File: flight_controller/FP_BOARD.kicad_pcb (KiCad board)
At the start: 2 copper layers, 100 x 100 mm, 252 parts, among them CN1 A1251WV-S-6P, CN2 A1251WV-S-4P, CN3 A1251WV-S-3P, J1 HX PZ2.54-3X4P ZZ, J10 A2012WV-S-9P, J11 A1257WV-S-6P-LCP, J12 A1257WV-S-6P-LCP, J13 A1257WV-S-6P-LCP, J14 HR911105A_C12074, J15 A1257WV-S-6P-LCP, J16 HCZZ0494-2, J17 TYPE-C16PIN2MD(073) (USB TYPE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, J2 B3B-ZR-SM4-TF(LF)(SN), J3 HX PZ2.54-3X4P ZZ, J4 HX PZ2.54-3X4P ZZ, J5 SM04B-SRSS-TB(LF)(SN), J6 A1257WV-S-6P-LCP, J7 HCZZ0494-4, J8 HCZZ0494-4, J9 A1257WV-S-6P-LCP, Q1 AO3400A, SW1 6.0*6.0*6.0, SW2 6.0*6.0*6.0, U1 HB-PH9-12727PB2GOB, U10 24LC64-I/SN, U11 FM25V02A-GTR, U12 MPU6500, U13 MS561101BA03-50, U14 LAN8742AI-CZ, U15 SN74LVC1G07DBVR_C19829659, U2 STM32H743IIT6, U3 HB-PH9-12727PB2GOB, U4 STM32F103C8T6, U5 SN74LVC2G240DCTR, U7 TJA1051T/3/1J, U8 TJA1051T/3/1J, U9 W25Q512JVFIQ, X1 XKXEL89CLI-SUAYLC-32.768K, X2 XL2EL89CLI-111YLC-16M, X3 X322524MLB4SI_C5210646, X4 XL2EL89CMI-111YLC-25M

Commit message: Placment in progress
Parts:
- moved R41 769.3 mm to (97.8, 42.6), turned to 180 degrees
- moved J2 741.5 mm to (97.5, 36.7), turned to 180 degrees
- moved R32 693.1 mm to (158.0, 48.6), turned to 180 degrees
- moved J1 687.2 mm to (149.2, 49.1), turned to 90 degrees
- moved R28 621.2 mm to (234.7, 31.9)
- moved R27 619.9 mm to (234.8, 35.1)
- moved R30 615.1 mm to (239.3, 35.6)
- moved U5 613.5 mm to (238.2, 26.4)
- moved R29 608.6 mm to (239.3, 32.1)
- moved C37 604.0 mm to (260.8, 24.7)
- moved J4 604.0 mm to (239.0, 45.2)
- moved R26 604.0 mm to (235.1, 57.6)
- moved R34 604.0 mm to (260.4, 52.3)
- moved R36 604.0 mm to (268.9, 29.8)
- moved R40 604.0 mm to (264.3, 52.3)
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
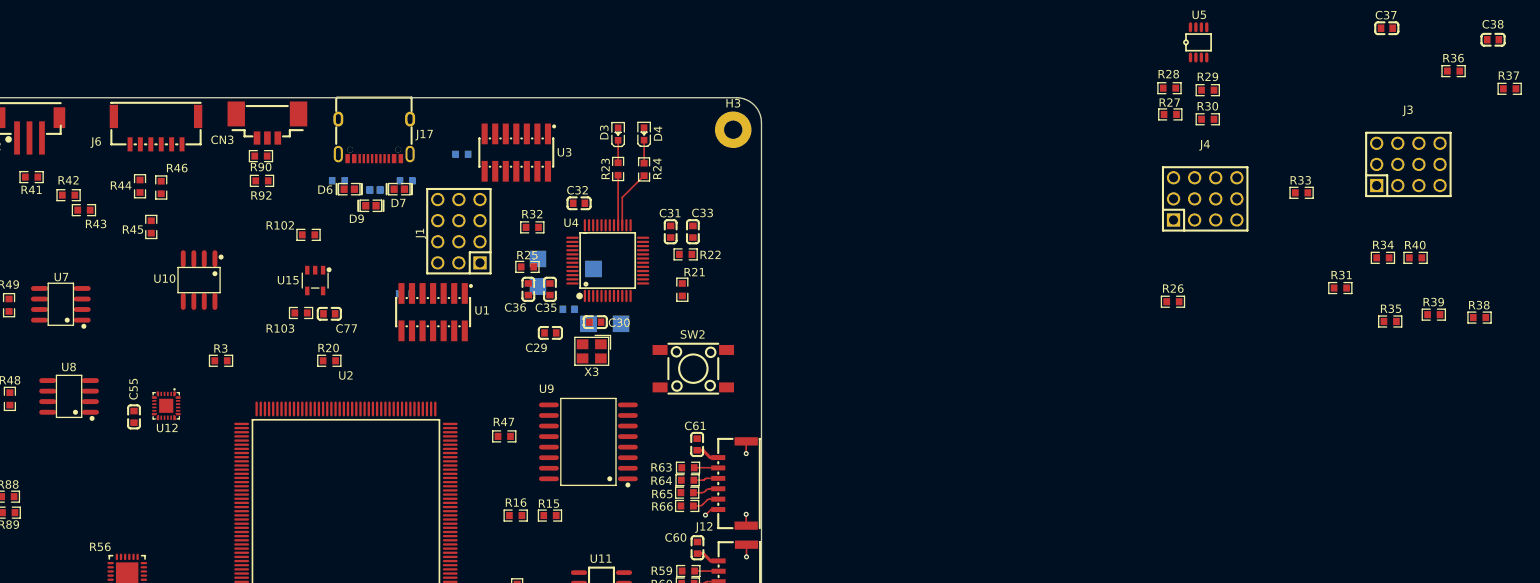
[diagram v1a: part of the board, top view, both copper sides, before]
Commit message: Almost done with placement , fixed some 3d models , fixed r56 to u56
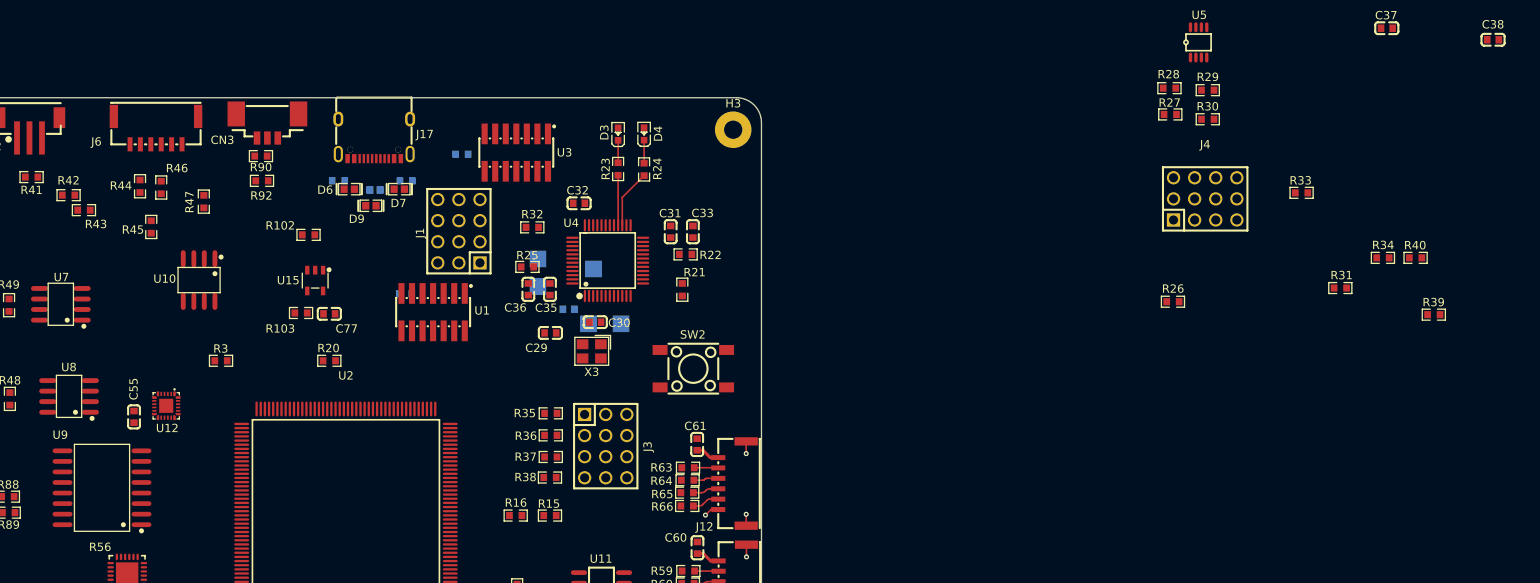
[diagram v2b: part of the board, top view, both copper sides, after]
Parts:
- moved R37 123.6 mm to (160.2, 76.3)
- moved R36 117.1 mm to (160.2, 73.7)
- moved R38 113.5 mm to (160.2, 78.8)
- moved J3 102.4 mm to (166.9, 75.0), turned to -90 degrees
- moved R35 101.6 mm to (160.2, 71.0)
- moved U9 58.8 mm to (106.2, 80.0)
- moved R47 45.9 mm to (118.5, 45.5), turned to 90 degrees

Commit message: Finished placement
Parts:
- removed R56: ICM-20689, easyeda2kicad:QFN-24_L4.0-W4.0-P0.50-TL-EP2.6
- added U56: ICM-20689, easyeda2kicad:QFN-24_L4.0-W4.0-P0.50-TL-EP2.6, F.Cu at (107.4, 91.1)
- C1, C2, R10, R15, R16, R17, R18, R92, R93, TP1, TP10, TP11, TP12, TP2, TP3, TP4, TP5, TP6, TP7, TP8, TP9, X1: moved to B.Cu
- moved C38 180.7 mm to (93.5, 40.7)
- moved TP11 159.1 mm to (151.7, 74.3), turned to 180 degrees
- moved TP8 153.8 mm to (151.4, 87.8), turned to 180 degrees
- moved R52 153.7 mm to (108.5, 117.5), turned to -90 degrees
- moved C54 151.8 mm to (113.0, 73.6), turned to 90 degrees
- moved R51 151.8 mm to (115.5, 77.5), turned to -90 degrees
- moved C17 151.0 mm to (125.6, 68.0)
- moved C50 149.6 mm to (120.5, 60.0), turned to 180 degrees
- moved TP4 149.0 mm to (144.7, 92.5), turned to 180 degrees
- moved TP9 148.9 mm to (151.6, 82.8), turned to 180 degrees
- moved R7 147.8 mm to (154.4, 67.0)
- moved TP10 147.5 mm to (144.1, 79.2), turned to 180 degrees
- moved TP6 147.4 mm to (151.4, 91.3), turned to 180 degrees
- moved TP12 147.2 mm to (149.8, 77.8), turned to 180 degrees
- moved R54 145.9 mm to (109.1, 103.0)
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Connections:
- Card1 pad 1: /SDMMC2_D2 -> /SENSORS/SDMMC2_D2
- Card1 pad 2: /SDMMC2_D3 -> /SENSORS/SDMMC2_D3
- Card1 pad 3: /SDMMC2_CMD -> /SENSORS/SDMMC2_CMD
- Card1 pad 5: /SDMMC2_CLK -> /SENSORS/SDMMC2_CLK
- Card1 pad 7: /SDMMC2_D0 -> /SENSORS/SDMMC2_D0
- Card1 pad 8: /SDMMC2_D1 -> /SENSORS/SDMMC2_D1
- Card1 pad 9: /SD_CARD_DETECT -> /SENSORS/SD_CARD_DETECT
- D8 pad 2: /USB_OTG_FS_DM -> /USB_OTG_FS_D-
- D9 pad 2: /USB_OTG_FS_DP -> /USB_OTG_FS_D+
- J17 pad 5: /USB_OTG_FS_DM -> /USB_OTG_FS_D-
- J17 pad 6: /USB_OTG_FS_DP -> /USB_OTG_FS_D+
- J17 pad 7: /USB_OTG_FS_DM -> /USB_OTG_FS_D-
- J17 pad 8: /USB_OTG_FS_DP -> /USB_OTG_FS_D+
- R50 pad 1: /SDMMC2_D2 -> /SENSORS/SDMMC2_D2
- R51 pad 1: /QUADSPI_BK1_NCS -> /SENSORS/QUADSPI_BK1_NCS
- R52 pad 1: /SDMMC2_D3 -> /SENSORS/SDMMC2_D3
- R53 pad 1: /SDMMC2_CMD -> /SENSORS/SDMMC2_CMD
- R54 pad 1: /SDMMC2_D0 -> /SENSORS/SDMMC2_D0
- R55 pad 1: /SDMMC2_D1 -> /SENSORS/SDMMC2_D1
- R57 pad 1: /I2C2_SDA -> /SENSORS/I2C2_SDA
- R58 pad 1: /I2C2_SCL -> /SENSORS/I2C2_SCL
- U10 pad 5: /I2C3_SDA -> /SENSORS/I2C3_SDA_EEPROM
- U10 pad 6: /I2C3_SCL -> /SENSORS/I2C3_SCL_EEPROM
- U11 pad 1: /SPI5_nCS1 -> /SENSORS/SPI5_nCS1
- U11 pad 2: /SPI5_MISO -> /SENSORS/SPI5_MISO
- U11 pad 5: /SPI5_MOSI -> /SENSORS/SPI5_MOSI
- U11 pad 6: /SPI5_SCK -> /SENSORS/SPI5_SCK
- U12 pad 12: /SPI2_DRDY2_INT2 -> /SENSORS/SPI2_DRDY2_INT2
- U12 pad 22: /SPI2_nCS1 -> /SENSORS/SPI2_nCS1
- U12 pad 23: /SPI2_SCK -> /SENSORS/SPI2_SCK
- U12 pad 24: /SPI2_MOSI -> /SENSORS/SPI2_MOSI
- U12 pad 9: /SPI2_MISO -> /SENSORS/SPI2_MISO
- U13 pad 7: /I2C2_SDA -> /SENSORS/I2C2_SDA
- U13 pad 8: /I2C2_SCL -> /SENSORS/I2C2_SCL
- U2 pad 122: /USB_OTG_FS_DM -> /STM32H7/USB_OTG_FS_D-
- U2 pad 123: /USB_OTG_FS_DP -> /STM32H7/USB_OTG_FS_D+
- U9 pad 1: /QUADSPI_BK1_IO3 -> /SENSORS/QUADSPI_BK1_IO3
- U9 pad 15: /QUADSPI_BK1_IO0 -> /SENSORS/QUADSPI_BK1_IO0
- U9 pad 16: /QUADSPI_CLK -> /SENSORS/QUADSPI_CLK
- U9 pad 7: /QUADSPI_BK1_NCS -> /SENSORS/QUADSPI_BK1_NCS
- U9 pad 8: /QUADSPI_BK1_IO1 -> /SENSORS/QUADSPI_BK1_IO1
- U9 pad 9: /QUADSPI_BK1_IO2 -> /SENSORS/QUADSPI_BK1_IO2
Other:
- copper layers 2 -> 6

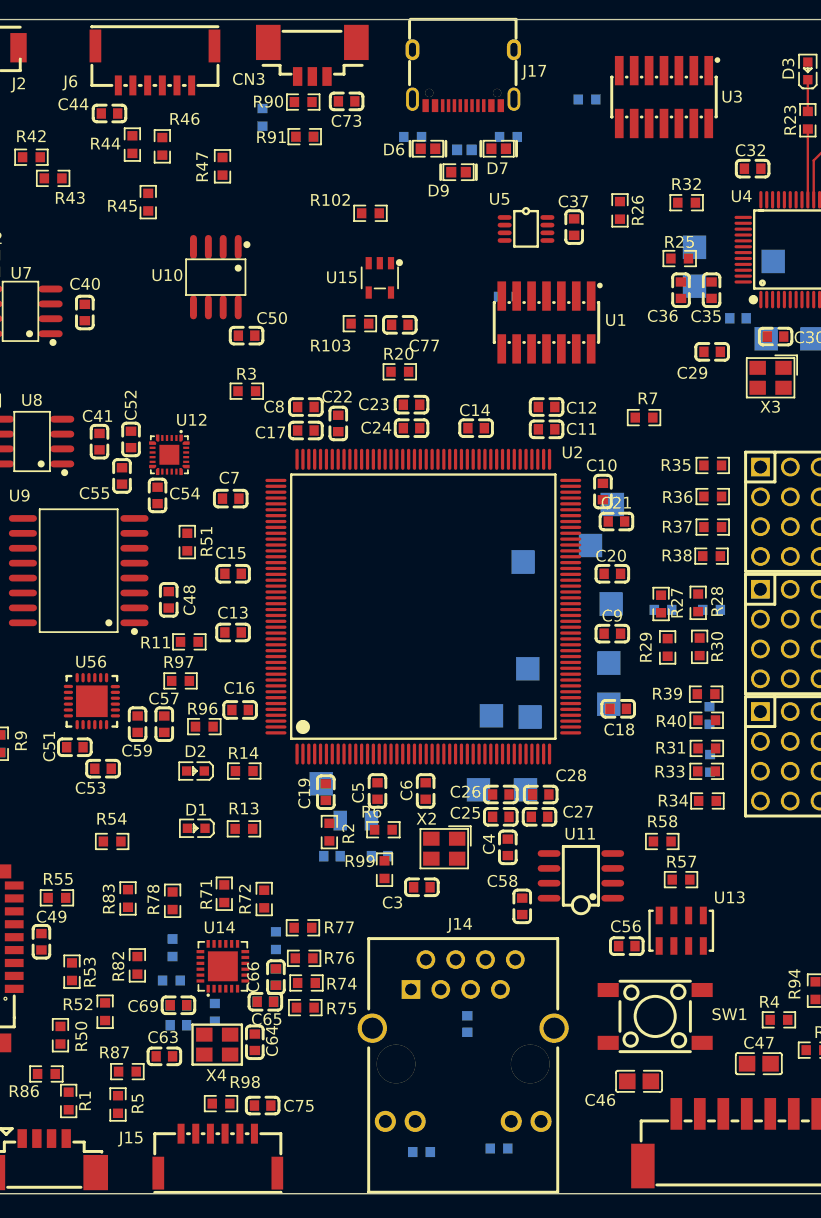
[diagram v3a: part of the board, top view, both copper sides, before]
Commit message: moved all to components to top
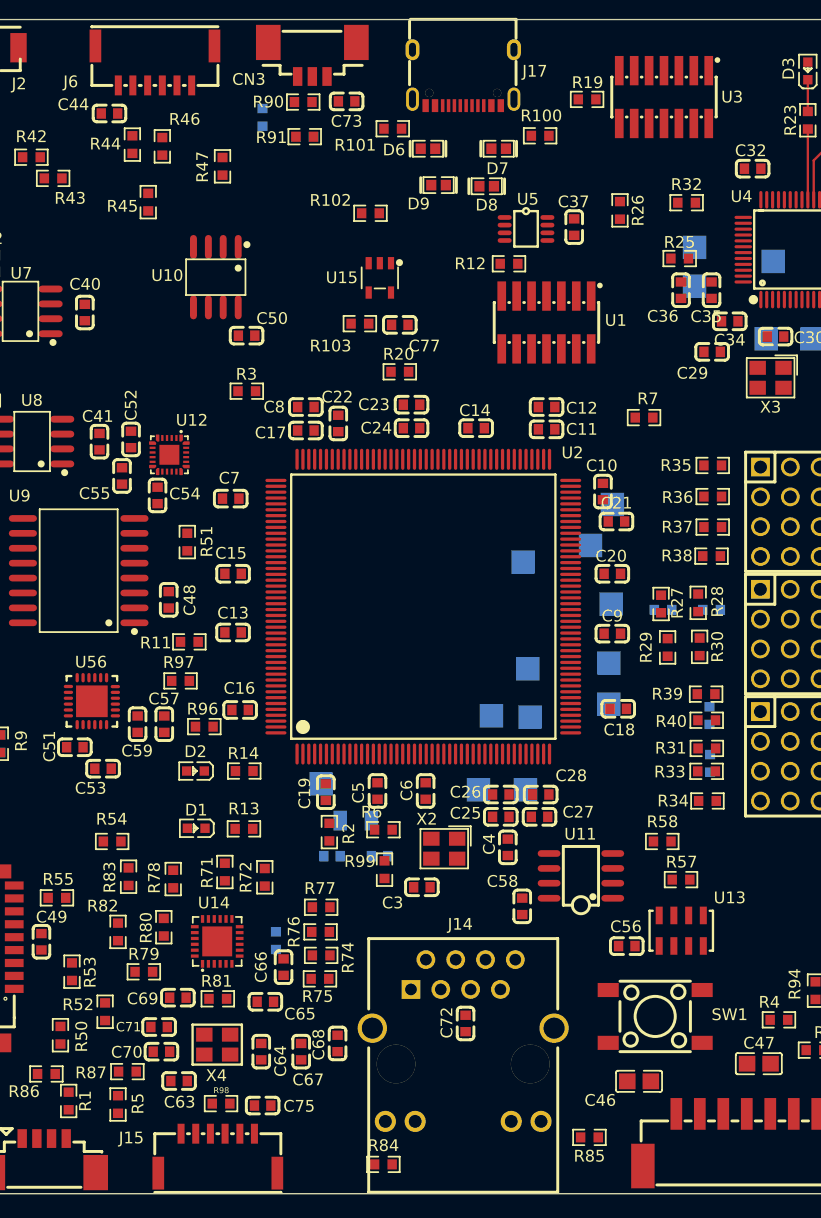
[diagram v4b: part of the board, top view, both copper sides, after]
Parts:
- C34, C67, C68, C70, C71, C72, D8, R100, R101, R12, R19, R79, R80, R81, R84, R85: moved to F.Cu
- moved R85 7.76 mm to (149.8, 128.2), turned to 180 degrees
- moved C68 7.71 mm to (128.3, 120.2)
- moved C67 5.23 mm to (125.2, 121.0), turned to 90 degrees
- moved C70 4.21 mm to (113.3, 121.0), turned to 180 degrees
- moved D8 3.64 mm to (141.0, 47.2), turned to 180 degrees
- moved R84 3.42 mm to (132.2, 130.6), turned to 0 degrees
- moved R82 3.29 mm to (109.6, 110.8)
- moved R12 2.80 mm to (142.9, 53.9), turned to 0 degrees
- moved R75 2.75 mm to (126.8, 114.8)
- moved R100 2.70 mm to (145.6, 43.0), turned to 0 degrees
- moved R74 2.66 mm to (126.9, 112.8)
- moved R76 2.65 mm to (126.8, 110.8)
- moved R79 2.47 mm to (111.8, 114.2), turned to 0 degrees
- moved C63 2.44 mm to (114.8, 123.5)
- moved R77 2.34 mm to (126.9, 108.7)
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
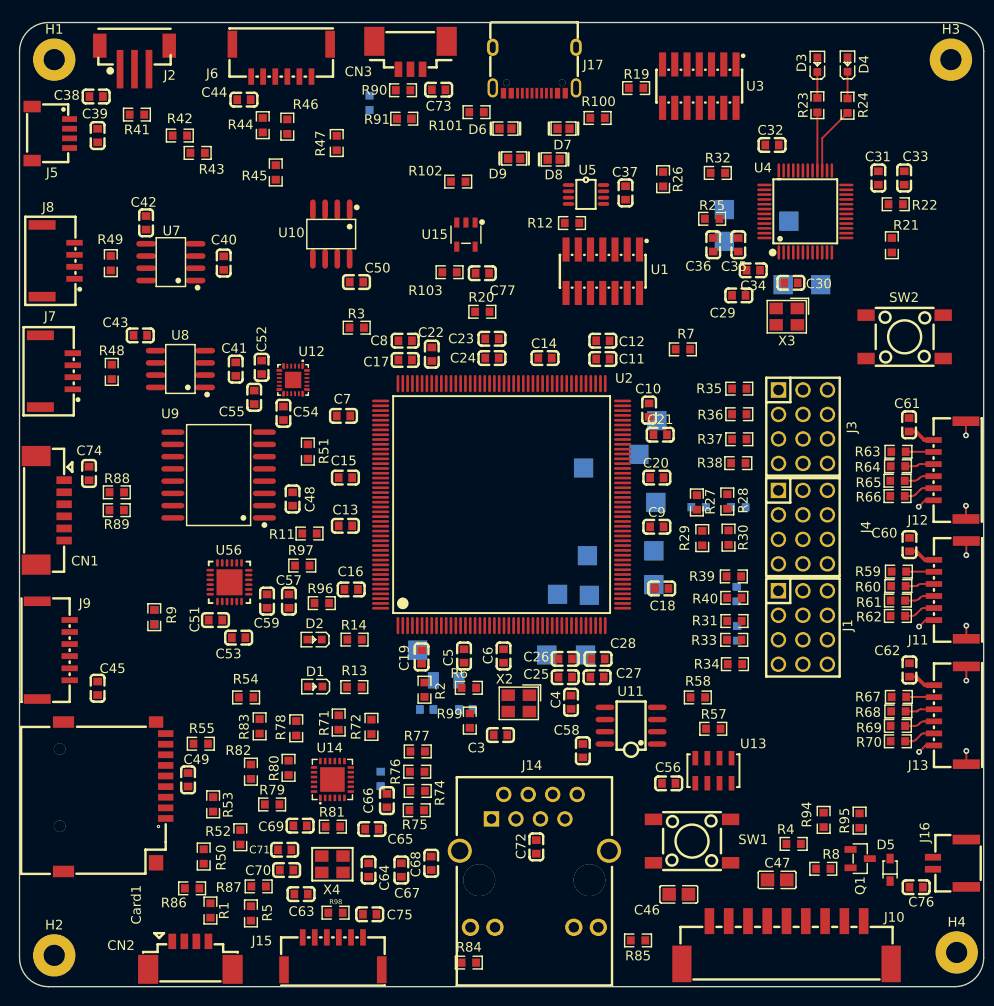
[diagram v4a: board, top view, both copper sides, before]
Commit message: renamed some connectors to j instead of cn
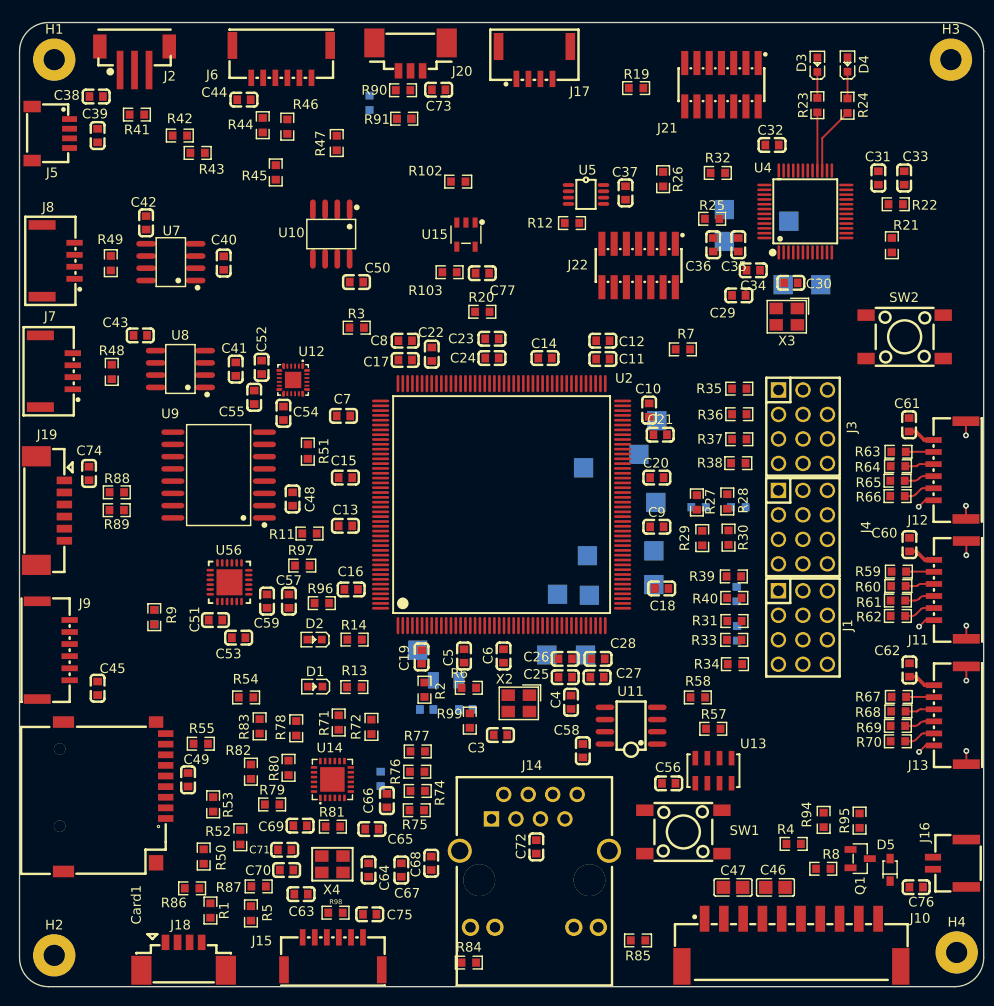
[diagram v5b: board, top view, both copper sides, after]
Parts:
- removed CN1: A1251WV-S-6P, easyeda2kicad:CONN-SMD_6P-P1.25_A1251WV-S-6P
- removed CN2: A1251WV-S-4P, easyeda2kicad:CONN-SMD_4P-P1.25_A1251WV-S-4P
- removed CN3: A1251WV-S-3P, easyeda2kicad:CONN-SMD_3P-P1.25_A1251WV-S-3P
- removed D6, D7, D8, D9: 0603ESDA-05N, easyeda2kicad:D0603-BI
- removed R100, R101: 0603WAF5101T5E, easyeda2kicad:R0603
- removed U1, U3: HB-PH9-12727PB2GOB, easyeda2kicad:HDR-SMD_14P-P1.27-V-M-R2-C7-LS5.5
- added J18: A1251WV-S-4P, easyeda2kicad:CONN-SMD_4P-P1.25_A1251WV-S-4P, F.Cu at (102.6, 129.9)
- added J19: A1251WV-S-6P, easyeda2kicad:CONN-SMD_6P-P1.25_A1251WV-S-6P, F.Cu at (88.8, 83.7)
- added J20: A1251WV-S-3P, easyeda2kicad:CONN-SMD_3P-P1.25_A1251WV-S-3P, F.Cu at (126.2, 36.6)
- added J21: HB-PH9-12727PB2GOB, easyeda2kicad:HDR-SMD_14P-P1.27-V-M-R2-C7-LS5.5, F.Cu at (158.4, 39.5)
- added J22: HB-PH9-12727PB2GOB, easyeda2kicad:HDR-SMD_14P-P1.27-V-M-R2-C7-LS5.5, F.Cu at (149.8, 58.2)
- J10: value A2012WV-S-9P -> CNJMA2012WV-S-10P; footprint easyeda2kicad:CONN-SMD_A2012WV-S-9P -> easyeda2kicad:CONN-SMD_10P-P2.00_CNJM_CNJMA2012WV-S-10P
- J17: value TYPE-C16PIN2MD(073) (USB TYPE C 16P) -> HCZZ0494-4; footprint easyeda2kicad:USB-C-SMD_TYPE-C-6PIN-2MD-073 -> easyeda2kicad:CONN-SMD_4P-P1.25_BM04B-GHS-TBT-LF-SN
- moved C46 10.1 mm to (164.0, 122.8)
- moved C47 4.64 mm to (159.6, 122.8)
- moved SW1 1.31 mm to (154.4, 117.0)
- moved J17 0.78 mm to (139.0, 37.2)
- moved J10 0.50 mm to (165.7, 128.5)
- moved J6 0.13 mm to (112.8, 37.1)
- moved J2 0.09 mm to (97.5, 36.8)
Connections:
- Card1 pad 1: /SENSORS/SDMMC2_D2 -> /SDMMC2_D2
- Card1 pad 2: /SENSORS/SDMMC2_D3 -> /SDMMC2_D3
- Card1 pad 3: /SENSORS/SDMMC2_CMD -> /SDMMC2_CMD
- Card1 pad 5: /SENSORS/SDMMC2_CLK -> /SDMMC2_CLK
- Card1 pad 7: /SENSORS/SDMMC2_D0 -> /SDMMC2_D0
- Card1 pad 8: /SENSORS/SDMMC2_D1 -> /SDMMC2_D1
- Card1 pad 9: /SENSORS/SD_CARD_DETECT -> /SD_CARD_DETECT
- J10 pad 1: 3V3 -> 5V
- J10 pad 2: 3V3 -> 5V
- J10 pad 3: 5V -> GND
- J10 pad 4: 5V -> GND
- J10 pad 5: /I2C4_SCL -> 3V3
- J10 pad 6: /I2C4_SDA -> 3V3
- J10 pad 7: /PWR_GPIO1 -> GND
- J10 pad 9: GND -> /I2C4_SCL
- J17 pad 1: GND -> /USB/USB_5V
- J17 pad 2: /USB/USB_5V -> /USB_OTG_FS_D-
- J17 pad 3: unconnected-(J17-SBU2-Pad3) -> /USB_OTG_FS_D+
- J17 pad 4: /USB/CC1 -> GND
- J17 pad 5: /USB_OTG_FS_D- -> GND
- J17 pad 6: /USB_OTG_FS_D+ -> GND
- R50 pad 1: /SENSORS/SDMMC2_D2 -> /SDMMC2_D2
- R51 pad 1: /SENSORS/QUADSPI_BK1_NCS -> /QUADSPI_BK1_NCS
- R52 pad 1: /SENSORS/SDMMC2_D3 -> /SDMMC2_D3
- R53 pad 1: /SENSORS/SDMMC2_CMD -> /SDMMC2_CMD
- R54 pad 1: /SENSORS/SDMMC2_D0 -> /SDMMC2_D0
- R55 pad 1: /SENSORS/SDMMC2_D1 -> /SDMMC2_D1
- R57 pad 1: /SENSORS/I2C2_SDA -> /I2C2_SDA
- R58 pad 1: /SENSORS/I2C2_SCL -> /I2C2_SCL
- U10 pad 5: /SENSORS/I2C3_SDA_EEPROM -> /I2C3_SDA
- U10 pad 6: /SENSORS/I2C3_SCL_EEPROM -> /I2C3_SCL
- U11 pad 1: /SENSORS/SPI5_nCS1 -> /SPI5_nCS1
- U11 pad 2: /SENSORS/SPI5_MISO -> /SPI5_MISO
- U11 pad 5: /SENSORS/SPI5_MOSI -> /SPI5_MOSI
- U11 pad 6: /SENSORS/SPI5_SCK -> /SPI5_SCK
- U12 pad 12: /SENSORS/SPI2_DRDY2_INT2 -> /SPI2_DRDY2_INT2
- U12 pad 22: /SENSORS/SPI2_nCS1 -> /SPI2_nCS1
- U12 pad 23: /SENSORS/SPI2_SCK -> /SPI2_SCK
- U12 pad 24: /SENSORS/SPI2_MOSI -> /SPI2_MOSI
- U12 pad 9: /SENSORS/SPI2_MISO -> /SPI2_MISO
- U13 pad 7: /SENSORS/I2C2_SDA -> /I2C2_SDA
- U13 pad 8: /SENSORS/I2C2_SCL -> /I2C2_SCL
- U2 pad 106: /PWR_GPIO1 -> /STM32H7/nPOWER_IN_B
- U2 pad 122: /STM32H7/USB_OTG_FS_D- -> /USB_OTG_FS_D-
- U2 pad 123: /STM32H7/USB_OTG_FS_D+ -> /USB_OTG_FS_D+
- U56 pad 12: /SENSORS/SPI1_DRDY1 -> /SPI1_DRDY1
- U56 pad 22: /SENSORS/SPI1_nCS1 -> /SPI1_nCS1
- U56 pad 23: /SENSORS/SPI1_SCK -> /SPI1_SCK
- U56 pad 24: /SENSORS/SPI1_MOSI -> /SPI1_MOSI
- U56 pad 9: /SENSORS/SPI1_MISO -> /SPI1_MISO
- U9 pad 1: /SENSORS/QUADSPI_BK1_IO3 -> /QUADSPI_BK1_IO3
- U9 pad 15: /SENSORS/QUADSPI_BK1_IO0 -> /QUADSPI_BK1_IO0
- U9 pad 16: /SENSORS/QUADSPI_CLK -> /QUADSPI_CLK
- U9 pad 7: /SENSORS/QUADSPI_BK1_NCS -> /QUADSPI_BK1_NCS
- U9 pad 8: /SENSORS/QUADSPI_BK1_IO1 -> /QUADSPI_BK1_IO1
- U9 pad 9: /SENSORS/QUADSPI_BK1_IO2 -> /QUADSPI_BK1_IO2
